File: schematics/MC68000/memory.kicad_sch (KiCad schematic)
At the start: 18 parts, among them J1 Conn_02x37_Row_Letter_Last, U13 ROM_LOW, U14 ROM_HIGH, U15 RAM_LOW, U16 RAM_HIGH, U17 GAL20V8, U26 74LS04, U27 74LS574

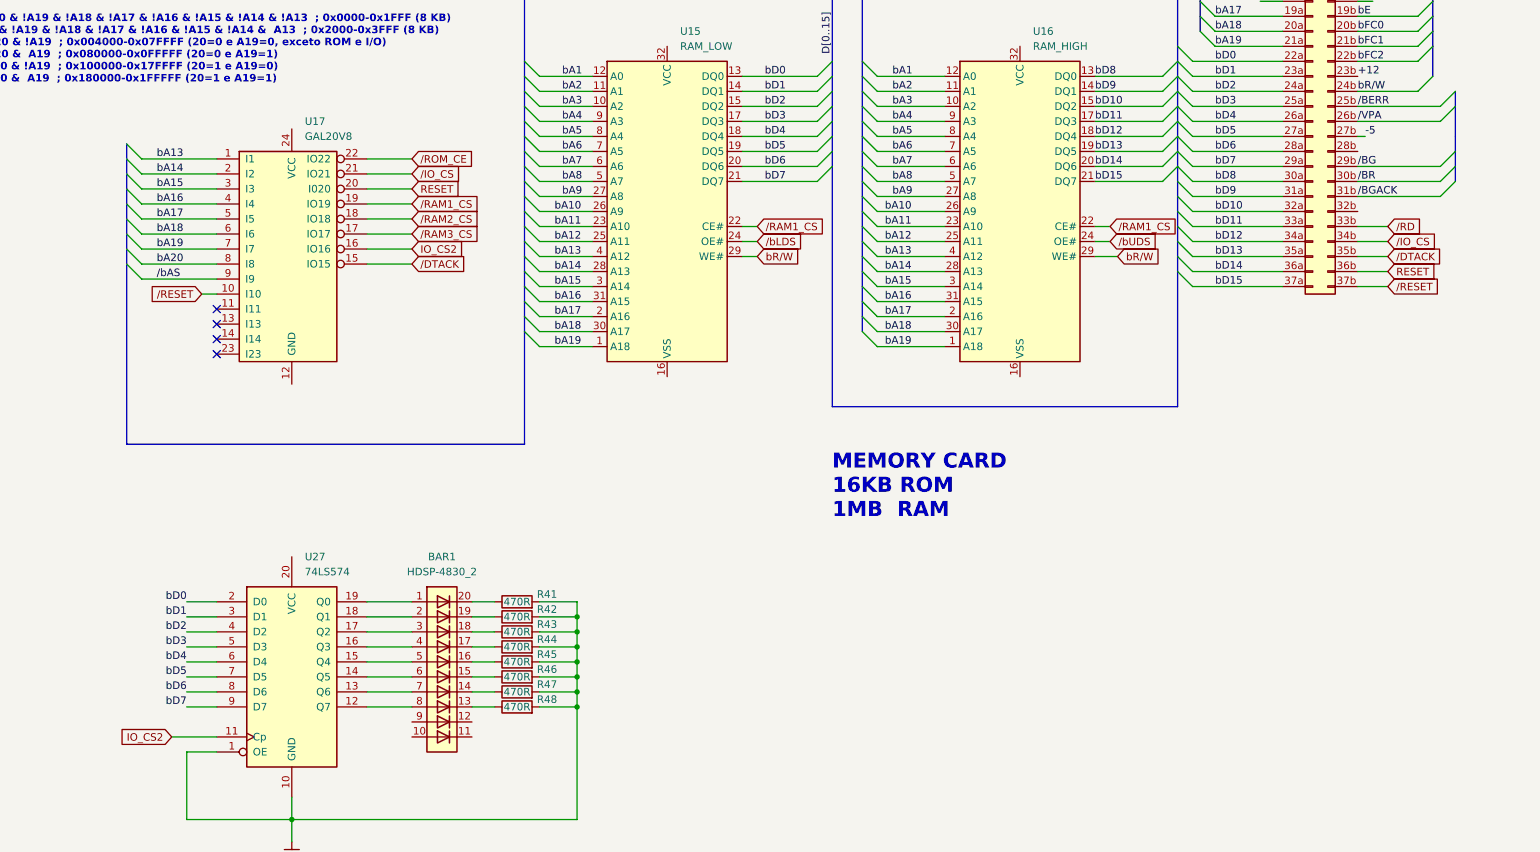
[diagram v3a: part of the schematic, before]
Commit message: Uart reading writing with counter.asm
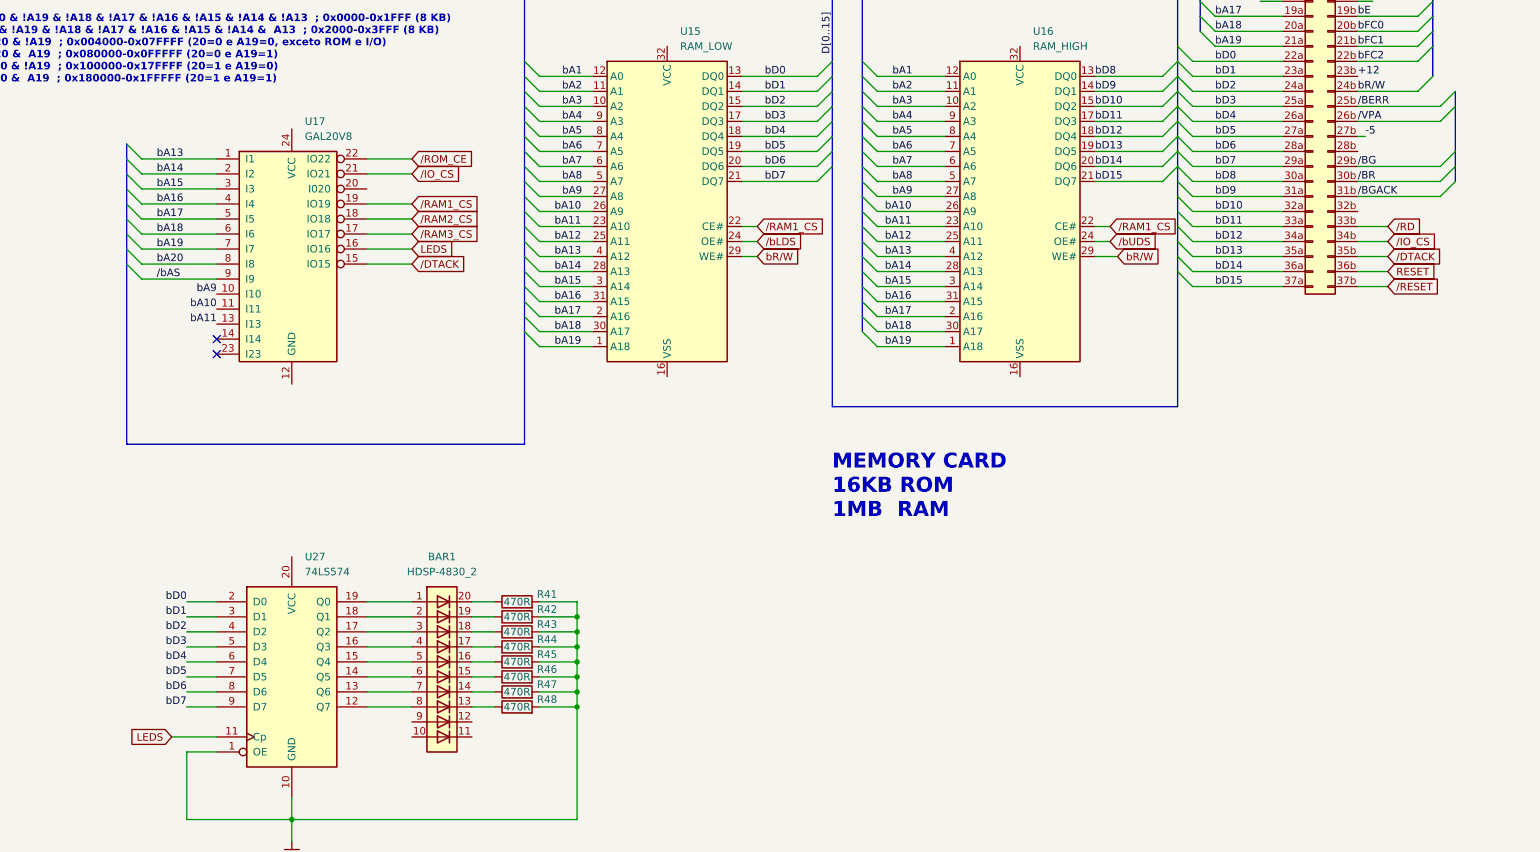
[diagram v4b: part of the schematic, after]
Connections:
- net RESET: no longer U17.20 (I020)
- net bA10: now also U17.11 (I11)
- net bA11: now also U17.13 (I13)
- net bA9: now also U17.10 (I10)
- net /RESET: no longer U17.10 (I10)
- net IO_CS2 renamed LEDS
- no-connect marks 6 -> 4
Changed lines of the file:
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@@
   (no_connect (at 73.66 148.59))
   (no_connect (at 140.97 64.77))
-  (no_connect (at 73.66 146.05))
-  (no_connect (at 73.66 143.51))
   (bus_entry (at 177.8 116.84) (size -2.54 2.54)
     (stroke (width 0) (type default))
@@
     (stroke (width 0) (type default))
   )
-  (bus (pts (xy 283.21 114.3) (xy 283.21 116.84))
+  (bus (pts (xy 283.21 109.22) (xy 283.21 116.84))
     (stroke (width 0) (type default))
   )
@@
     (stroke (width 0) (type default))
   )
-  (wire (pts (xy 71.12 140.97) (xy 73.66 140.97))
-    (stroke (width 0) (type default))
-  )
   (bus (pts (xy 240.03 78.74) (xy 240.03 81.28))
     (stroke (width 0) (type default))
@@
     (stroke (width 0) (type default))
   )
-  (wire (pts (xy 106.68 123.19) (xy 99.06 123.19))
-    (stroke (width 0) (type default))
-  )
   (bus (pts (xy 240.03 45.72) (xy 240.03 48.26))
     (stroke (width 0) (type default))
@@
   )
   (bus (pts (xy 125.73 49.53) (xy 125.73 52.07))
-    (stroke (width 0) (type default))
-  )
-  (bus (pts (xy 283.21 109.22) (xy 283.21 114.3))
     (stroke (width 0) (type default))
   )
@@
     (effects (font (size 1.27 1.27)) (justify left bottom))
   )
+  (label "bA9" (at 73.66 140.97 180) (fields_autoplaced)
+    (effects (font (size 1.27 1.27)) (justify right bottom))
+  )
   (label "bFC2" (at 266.7 101.6 0) (fields_autoplaced)
     (effects (font (size 1.27 1.27)) (justify left bottom))
@@
     (effects (font (size 1.27 1.27)) (justify left bottom))
   )
+  (label "bA11" (at 73.66 146.05 180) (fields_autoplaced)
+    (effects (font (size 1.27 1.27)) (justify right bottom))
+  )
   (label "bA17" (at 63.5 128.27 0) (fields_autoplaced)
     (effects (font (size 1.27 1.27)) (justify left bottom))
@@
   (label "bR{slash}W" (at 281.94 87.63 90) (fields_autoplaced)
     (effects (font (size 1.27 1.27)) (justify left bottom))
+  )
+  (label "bA10" (at 73.66 143.51 180) (fields_autoplaced)
+    (effects (font (size 1.27 1.27)) (justify right bottom))
   )
   (label "bD15" (at 222.25 121.92 0) (fields_autoplaced)
@@
     )
   )
-  (global_label "IO_CS2" (shape input) (at 66.04 215.9 180) (fields_autoplaced)
+  (global_label "LEDS" (shape input) (at 66.04 215.9 180) (fields_autoplaced)
     (effects (font (size 1.27 1.27)) (justify right))
-    (property "Intersheetrefs" "${INTERSHEET_REFS}" (at 56.4629 215.9 0)
+    (property "Intersheetrefs" "${INTERSHEET_REFS}" (at 58.3982 215.9 0)
       (effects (font (size 1.27 1.27)) (justify right) hide)
     )
@@
     )
   )
-  (global_label "{slash}RESET" (shape input) (at 71.12 140.97 180) (fields_autoplaced)
-    (effects (font (size 1.27 1.27)) (justify right))
-    (property "Intersheetrefs" "${INTERSHEET_REFS}" (at 61.0592 140.97 0)
-      (effects (font (size 1.27 1.27)) (justify right) hide)
-    )
-  )
   (global_label "bR{slash}W" (shape input) (at 165.1 134.62 0) (fields_autoplaced)
     (effects (font (size 1.27 1.27)) (justify left))
@@
     )
   )
-  (global_label "IO_CS2" (shape input) (at 106.68 133.35 0) (fields_autoplaced)
+  (global_label "LEDS" (shape input) (at 106.68 133.35 0) (fields_autoplaced)
     (effects (font (size 1.27 1.27)) (justify left))
-    (property "Intersheetrefs" "${INTERSHEET_REFS}" (at 116.2571 133.35 0)
+    (property "Intersheetrefs" "${INTERSHEET_REFS}" (at 114.3218 133.35 0)
       (effects (font (size 1.27 1.27)) (justify left) hide)
     )
@@
       (effects (font (size 1.27 1.27)) (justify left) hide)
     )
-  )
-  (global_label "RESET" (shape input) (at 106.68 123.19 0) (fields_autoplaced)
-    (effects (font (size 1.27 1.27)) (justify left))
-    (property "Intersheetrefs" "${INTERSHEET_REFS}" (at 115.4103 123.19 0)
-      (effects (font (size 1.27 1.27)) (justify left) hide)
-    )

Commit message: Updating...
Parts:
- removed U26: 74LS04, symbol 74xx:74LS04
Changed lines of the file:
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@@
-    )
-  )
-  (symbol (lib_id "74xx:74LS04") (at 50.8 270.51 0) (unit 2)
-    (in_bom yes) (on_board yes) (dnp no) (fields_autoplaced)
-    (property "Reference" "U26" (at 50.8 261.62 0)
-      (effects (font (size 1.27 1.27)))
-    )
-    (property "Value" "74LS04" (at 50.8 264.16 0)
-      (effects (font (size 1.27 1.27)))
-    )
-    (property "Footprint" "" (at 50.8 270.51 0)
-      (effects (font (size 1.27 1.27)) hide)
-    )
-    (property "Datasheet" "http://www.ti.com/lit/gpn/sn74LS04" (at 50.8 270.51 0)
-      (effects (font (size 1.27 1.27)) hide)
-    )
-    (pin "11")
-    (pin "10")
-    (pin "1")
-    (pin "2")
-    (pin "5")
-    (pin "6")
-    (pin "13")
-    (pin "8")
-    (pin "4")
-    (pin "7")
-    (pin "3")
-    (pin "9")
-    (pin "12")
-    (pin "14")
-    (instances
-      (project "MC68000"
-        (path "/99c9748a-87b3-41bd-bdc2-3a5f137c7a40/46851f42-1a1d-4f27-b9e4-631920caffce"
-          (reference "U26") (unit 2)
-        )
-      )
-    )
-  )
-  (symbol (lib_id "74xx:74LS04") (at 74.93 270.51 0) (unit 3)
-    (in_bom yes) (on_board yes) (dnp no) (fields_autoplaced)
-    (property "Reference" "U26" (at 74.93 261.62 0)
-      (effects (font (size 1.27 1.27)))
-    )
-    (property "Value" "74LS04" (at 74.93 264.16 0)
-      (effects (font (size 1.27 1.27)))
-    )
-    (property "Footprint" "" (at 74.93 270.51 0)
-      (effects (font (size 1.27 1.27)) hide)
-    )
-    (property "Datasheet" "http://www.ti.com/lit/gpn/sn74LS04" (at 74.93 270.51 0)
-      (effects (font (size 1.27 1.27)) hide)
-    )
-    (pin "11")
-    (pin "10")
-    (pin "1")
-    (pin "2")
-    (pin "5")
-    (pin "6")
-    (pin "13")
-    (pin "8")
-    (pin "4")
-    (pin "7")
-    (pin "3")
-    (pin "9")
-    (pin "12")
-    (pin "14")
-    (instances
-      (project "MC68000"
-        (path "/99c9748a-87b3-41bd-bdc2-3a5f137c7a40/46851f42-1a1d-4f27-b9e4-631920caffce"
-          (reference "U26") (unit 3)
-        )
-      )
     )
   )
@@
     )
   )
-  (symbol (lib_id "74xx:74LS04") (at 170.18 267.97 0) (unit 7)
-    (in_bom yes) (on_board yes) (dnp no) (fields_autoplaced)
-    (property "Reference" "U26" (at 176.53 266.7 0)
-      (effects (font (size 1.27 1.27)) (justify left))
-    )
-    (property "Value" "74LS04" (at 176.53 269.24 0)
-      (effects (font (size 1.27 1.27)) (justify left))
-    )
-    (property "Footprint" "" (at 170.18 267.97 0)
-      (effects (font (size 1.27 1.27)) hide)
-    )
-    (property "Datasheet" "http://www.ti.com/lit/gpn/sn74LS04" (at 170.18 267.97 0)
-      (effects (font (size 1.27 1.27)) hide)
-    )
-    (pin "11")
-    (pin "10")
-    (pin "1")
-    (pin "2")
-    (pin "5")
-    (pin "6")
-    (pin "13")
-    (pin "8")
-    (pin "4")
-    (pin "7")
-    (pin "3")
-    (pin "9")
-    (pin "12")
-    (pin "14")
-    (instances
-      (project "MC68000"
-        (path "/99c9748a-87b3-41bd-bdc2-3a5f137c7a40/46851f42-1a1d-4f27-b9e4-631920caffce"
-          (reference "U26") (unit 7)
-        )
-      )
-    )
-  )
   (symbol (lib_id "Device:R") (at 124.46 203.2 90) (unit 1)
     (in_bom yes) (on_board yes) (dnp no)
@@
         (path "/99c9748a-87b3-41bd-bdc2-3a5f137c7a40/46851f42-1a1d-4f27-b9e4-631920caffce"
           (reference "R45") (unit 1)
-        )
-      )
-    )
-  )
-  (symbol (lib_id "74xx:74LS04") (at 143.51 270.51 0) (unit 6)
-    (in_bom yes) (on_board yes) (dnp no) (fields_autoplaced)
-    (property "Reference" "U26" (at 143.51 261.62 0)
-      (effects (font (size 1.27 1.27)))
-    )
-    (property "Value" "74LS04" (at 143.51 264.16 0)
-      (effects (font (size 1.27 1.27)))
-    )
-    (property "Footprint" "" (at 143.51 270.51 0)
-      (effects (font (size 1.27 1.27)) hide)
-    )
-    (property "Datasheet" "http://www.ti.com/lit/gpn/sn74LS04" (at 143.51 270.51 0)
-      (effects (font (size 1.27 1.27)) hide)
-    )
-    (pin "11")
-    (pin "10")
-    (pin "1")
-    (pin "2")
-    (pin "5")
-    (pin "6")
-    (pin "13")
-    (pin "8")
-    (pin "4")
-    (pin "7")
-    (pin "3")
-    (pin "9")
-    (pin "12")
-    (pin "14")
-    (instances
-      (project "MC68000"
-        (path "/99c9748a-87b3-41bd-bdc2-3a5f137c7a40/46851f42-1a1d-4f27-b9e4-631920caffce"
-          (reference "U26") (unit 6)
         )
       )
@@
         (path "/99c9748a-87b3-41bd-bdc2-3a5f137c7a40/46851f42-1a1d-4f27-b9e4-631920caffce"
           (reference "BAR1") (unit 1)
-        )
-      )
-    )
-  )
-  (symbol (lib_id "74xx:74LS04") (at 96.52 270.51 0) (unit 4)
-    (in_bom yes) (on_board yes) (dnp no) (fields_autoplaced)
-    (property "Reference" "U26" (at 96.52 261.62 0)
-      (effects (font (size 1.27 1.27)))
-    )
-    (property "Value" "74LS04" (at 96.52 264.16 0)
-      (effects (font (size 1.27 1.27)))
-    )
-    (property "Footprint" "" (at 96.52 270.51 0)
-      (effects (font (size 1.27 1.27)) hide)
-    )
-    (property "Datasheet" "http://www.ti.com/lit/gpn/sn74LS04" (at 96.52 270.51 0)
-      (effects (font (size 1.27 1.27)) hide)
-    )
-    (pin "11")
-    (pin "10")
-    (pin "1")
-    (pin "2")
-    (pin "5")
-    (pin "6")
-    (pin "13")
-    (pin "8")
-    (pin "4")
-    (pin "7")
-    (pin "3")
-    (pin "9")
-    (pin "12")
-    (pin "14")
-    (instances
-      (project "MC68000"
-        (path "/99c9748a-87b3-41bd-bdc2-3a5f137c7a40/46851f42-1a1d-4f27-b9e4-631920caffce"
-          (reference "U26") (unit 4)
         )
       )
@@
         )
       )
-    )
-  )
-  (symbol (lib_id "74xx:74LS04") (at 119.38 270.51 0) (unit 5)
-    (in_bom yes) (on_board yes) (dnp no) (fields_autoplaced)
-    (property "Reference" "U26" (at 119.38 261.62 0)
-      (effects (font (size 1.27 1.27)))
-    )
-    (property "Value" "74LS04" (at 119.38 264.16 0)
-      (effects (font (size 1.27 1.27)))
-    )
-    (property "Footprint" "" (at 119.38 270.51 0)
-      (effects (font (size 1.27 1.27)) hide)
-    )
-    (property "Datasheet" "http://www.ti.com/lit/gpn/sn74LS04" (at 119.38 270.51 0)
-      (effects (font (size 1.27 1.27)) hide)
-    )
-    (pin "11")
-    (pin "10")
-    (pin "1")
-    (pin "2")
-    (pin "5")
-    (pin "6")
-    (pin "13")
-    (pin "8")
-    (pin "4")
-    (pin "7")
-    (pin "3")
-    (pin "9")
-    (pin "12")
-    (pin "14")
-    (instances
-      (project "MC68000"
-        (path "/99c9748a-87b3-41bd-bdc2-3a5f137c7a40/46851f42-1a1d-4f27-b9e4-631920caffce"
-          (reference "U26") (unit 5)
-        )
-      )
